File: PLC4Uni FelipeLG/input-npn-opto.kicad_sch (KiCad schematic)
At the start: 3 parts

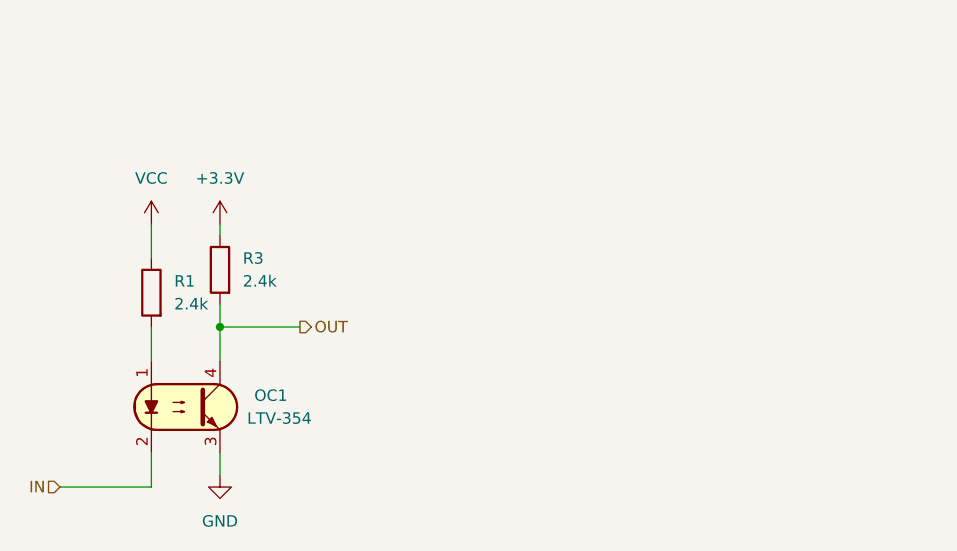
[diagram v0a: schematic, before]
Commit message: Add files via upload
Updated Circuitos corregidos y pistas agregadas
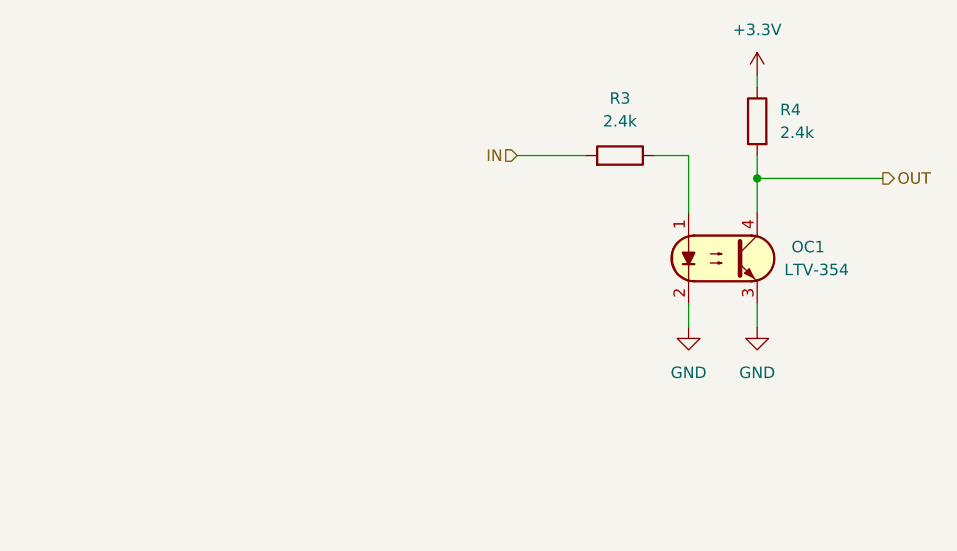
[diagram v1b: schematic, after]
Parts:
- removed R1: 2.4k, Resistor_SMD_AKL:R_0603_1608Metric, symbol Resistor_AKL:R_0603
- added R4: 2.4k, Resistor_SMD_AKL:R_0603_1608Metric, symbol Resistor_AKL:R_0603
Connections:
- net +3.3V: now also R4.2; no longer R3.2
- net GND: now also OC1.2
- net IN: now also R3.1; no longer OC1.2
- net OUT: now also R4.1; no longer R3.1
- net at OC1.1: now also R3.2
